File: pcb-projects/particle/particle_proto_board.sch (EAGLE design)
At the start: 38 parts, among them IC1 ATTINY20-MMH, IC2 DMC2400V, IC3 DMC2400V, J1 FTS-103-01-L-DV, SW1 T/S-PI SW, SW2 T/S-PI SW, SW3 T/S-PI SW

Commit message: closed #44, closed #43, closed #42
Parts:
- removed R11, R2: J5MM, jumper:J5MM
- removed R12: J15MM, jumper:J15MM
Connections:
- removed net N$17: IC3A.S, R11.1
- removed net N$2: R2.1, RXA.P
- net GND: now also IC3A.S; no longer R11.2
- net RX_A: now also RXA.P; no longer R2.2
- net VCC: no longer R12.1, R12.2
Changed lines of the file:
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@@
 <grid distance="0.1" unitdist="inch" unit="inch" style="lines" multiple="1" display="no" altdistance="0.01" altunitdist="inch" altunit="inch"/>
 <layers>
-<layer number="1" name="Top" color="4" fill="1" visible="yes" active="no"/>
-<layer number="16" name="Bottom" color="1" fill="1" visible="yes" active="no"/>
-<layer number="17" name="Pads" color="2" fill="1" visible="yes" active="no"/>
-<layer number="18" name="Vias" color="2" fill="1" visible="yes" active="no"/>
-<layer number="19" name="Unrouted" color="6" fill="1" visible="yes" active="no"/>
-<layer number="20" name="Dimension" color="15" fill="1" visible="yes" active="no"/>
-<layer number="21" name="tPlace" color="7" fill="1" visible="yes" active="no"/>
-<layer number="22" name="bPlace" color="7" fill="1" visible="yes" active="no"/>
-<layer number="23" name="tOrigins" color="15" fill="1" visible="yes" active="no"/>
-<layer number="24" name="bOrigins" color="15" fill="1" visible="yes" active="no"/>
-<layer number="25" name="tNames" color="7" fill="1" visible="yes" active="no"/>
-<layer number="26" name="bNames" color="7" fill="1" visible="yes" active="no"/>
-<layer number="27" name="tValues" color="7" fill="1" visible="yes" active="no"/>
-<layer number="28" name="bValues" color="7" fill="1" visible="yes" active="no"/>
+<layer number="1" name="Top" color="4" fill="1" visible="no" active="no"/>
+<layer number="16" name="Bottom" color="1" fill="1" visible="no" active="no"/>
+<layer number="17" name="Pads" color="2" fill="1" visible="no" active="no"/>
+<layer number="18" name="Vias" color="2" fill="1" visible="no" active="no"/>
+<layer number="19" name="Unrouted" color="6" fill="1" visible="no" active="no"/>
+<layer number="20" name="Dimension" color="15" fill="1" visible="no" active="no"/>
+<layer number="21" name="tPlace" color="7" fill="1" visible="no" active="no"/>
+<layer number="22" name="bPlace" color="7" fill="1" visible="no" active="no"/>
+<layer number="23" name="tOrigins" color="15" fill="1" visible="no" active="no"/>
+<layer number="24" name="bOrigins" color="15" fill="1" visible="no" active="no"/>
+<layer number="25" name="tNames" color="7" fill="1" visible="no" active="no"/>
+<layer number="26" name="bNames" color="7" fill="1" visible="no" active="no"/>
+<layer number="27" name="tValues" color="7" fill="1" visible="no" active="no"/>
+<layer number="28" name="bValues" color="7" fill="1" visible="no" active="no"/>
 <layer number="29" name="tStop" color="7" fill="3" visible="no" active="no"/>
 <layer number="30" name="bStop" color="7" fill="6" visible="no" active="no"/>
@@
 <layer number="35" name="tGlue" color="7" fill="4" visible="no" active="no"/>
 <layer number="36" name="bGlue" color="7" fill="5" visible="no" active="no"/>
-<layer number="37" name="tTest" color="7" fill="1" visible="yes" active="no"/>
-<layer number="38" name="bTest" color="7" fill="1" visible="yes" active="no"/>
+<layer number="37" name="tTest" color="7" fill="1" visible="no" active="no"/>
+<layer number="38" name="bTest" color="7" fill="1" visible="no" active="no"/>
 <layer number="39" name="tKeepout" color="4" fill="11" visible="no" active="no"/>
 <layer number="40" name="bKeepout" color="1" fill="11" visible="no" active="no"/>
@@
 <layer number="44" name="Drills" color="7" fill="1" visible="no" active="no"/>
 <layer number="45" name="Holes" color="7" fill="1" visible="no" active="no"/>
-<layer number="46" name="Milling" color="3" fill="1" visible="yes" active="no"/>
-<layer number="47" name="Measures" color="7" fill="1" visible="yes" active="no"/>
-<layer number="48" name="Document" color="7" fill="1" visible="yes" active="no"/>
-<layer number="49" name="Reference" color="7" fill="1" visible="yes" active="no"/>
-<layer number="50" name="dxf" color="7" fill="1" visible="yes" active="no"/>
-<layer number="51" name="tDocu" color="7" fill="1" visible="yes" active="no"/>
-<layer number="52" name="bDocu" color="7" fill="1" visible="yes" active="no"/>
-<layer number="53" name="tGND_GNDA" color="7" fill="9" visible="yes" active="no"/>
-<layer number="54" name="bGND_GNDA" color="1" fill="9" visible="yes" active="no"/>
-<layer number="56" name="wert" color="7" fill="1" visible="yes" active="no"/>
-<layer number="57" name="tCAD" color="7" fill="1" visible="yes" active="no"/>
+<layer number="46" name="Milling" color="3" fill="1" visible="no" active="no"/>
+<layer number="47" name="Measures" color="7" fill="1" visible="no" active="no"/>
+<layer number="48" name="Document" color="7" fill="1" visible="no" active="no"/>
+<layer number="49" name="Reference" color="7" fill="1" visible="no" active="no"/>
+<layer number="50" name="dxf" color="7" fill="1" visible="no" active="no"/>
+<layer number="51" name="tDocu" color="7" fill="1" visible="no" active="no"/>
+<layer number="52" name="bDocu" color="7" fill="1" visible="no" active="no"/>
+<layer number="53" name="tGND_GNDA" color="7" fill="9" visible="no" active="no"/>
+<layer number="54" name="bGND_GNDA" color="1" fill="9" visible="no" active="no"/>
+<layer number="56" name="wert" color="7" fill="1" visible="no" active="no"/>
+<layer number="57" name="tCAD" color="7" fill="1" visible="no" active="no"/>
 <layer number="90" name="Modules" color="5" fill="1" visible="yes" active="yes"/>
 <layer number="91" name="Nets" color="2" fill="1" visible="yes" active="yes"/>
@@
 <part name="PWR_LED" library="led" deviceset="LED" device="SML1206" value="RED"/>
 <part name="P+3" library="supply1" deviceset="VCC" device=""/>
-<part name="R11" library="jumper" deviceset="J" device="5MM" value=""/>
-<part name="P+5" library="supply1" deviceset="VCC" device=""/>
-<part name="P+7" library="supply1" deviceset="VCC" device=""/>
-<part name="R12" library="jumper" deviceset="J" device="15MM" value="J15MM"/>
 <part name="RESET" library="SparkFun-Electromechanical" deviceset="SWITCH-MOMENTARY-2" device="SMD"/>
 <part name="J1" library="samtec-FTS-103-01-L-DV" deviceset="FTS-103-01-L-DV" device=""/>
@@
 <part name="SW3" library="jumper-switches" deviceset="J2" device="X2MM" value="T/S-PI SW"/>
 <part name="SW2" library="jumper-switches" deviceset="J2" device="X2MM" value="T/S-PI SW"/>
-<part name="R2" library="jumper" deviceset="J" device="5MM" value="J5MM"/>
 </parts>
 <sheets>
@@
 <instance part="PWR_LED" gate="G$1" x="149.86" y="129.54"/>
 <instance part="P+3" gate="VCC" x="149.86" y="149.86"/>
-<instance part="R11" gate="1" x="297.18" y="86.36" rot="MR270"/>
-<instance part="P+5" gate="VCC" x="99.06" y="10.16" rot="R90"/>
-<instance part="P+7" gate="VCC" x="114.3" y="10.16" rot="R270"/>
-<instance part="R12" gate="1" x="106.68" y="10.16" rot="MR0"/>
 <instance part="RESET" gate="G$1" x="22.86" y="114.3" rot="R90"/>
 <instance part="J1" gate="A" x="124.46" y="48.26" rot="R180"/>
@@
 <instance part="SW3" gate="G$1" x="81.28" y="50.8" rot="R180"/>
 <instance part="SW2" gate="G$1" x="81.28" y="66.04" rot="R180"/>
-<instance part="R2" gate="1" x="241.3" y="147.32" rot="MR270"/>
 </instances>
 <busses>
@@
 </segment>
 <segment>
-<pinref part="R11" gate="1" pin="2"/>
 <pinref part="GND1" gate="1" pin="GND"/>
-<wire x1="297.18" y1="81.28" x2="297.18" y2="78.74" width="0.1524" layer="91"/>
+<pinref part="IC3" gate="A" pin="S"/>
+<wire x1="297.18" y1="93.98" x2="297.18" y2="78.74" width="0.1524" layer="91"/>
 </segment>
 <segment>
@@
 </segment>
 <segment>
-<pinref part="R12" gate="1" pin="1"/>
-<pinref part="P+7" gate="VCC" pin="VCC"/>
-</segment>
-<segment>
-<pinref part="R12" gate="1" pin="2"/>
-<pinref part="P+5" gate="VCC" pin="VCC"/>
-</segment>
-<segment>
 <pinref part="J1" gate="A" pin="2"/>
 <wire x1="106.68" y1="48.26" x2="104.14" y2="48.26" width="0.1524" layer="91"/>
@@
 <wire x1="210.82" y1="139.7" x2="210.82" y2="137.16" width="0.1524" layer="91"/>
 <junction x="210.82" y="137.16"/>
-<pinref part="R2" gate="1" pin="2"/>
-<wire x1="241.3" y1="137.16" x2="241.3" y2="142.24" width="0.1524" layer="91"/>
+<pinref part="RXA" gate="1" pin="P"/>
+<wire x1="241.3" y1="160.02" x2="241.3" y2="137.16" width="0.1524" layer="91"/>
 </segment>
 <segment>
@@
 </segment>
 </net>
-<net name="N$17" class="0">
-<segment>
-<pinref part="IC3" gate="A" pin="S"/>
-<pinref part="R11" gate="1" pin="1"/>
-<wire x1="297.18" y1="93.98" x2="297.18" y2="91.44" width="0.1524" layer="91"/>
-</segment>
-</net>
 <net name="N$23" class="0">
 <segment>
@@
 </segment>
 </net>
-<net name="N$2" class="0">
-<segment>
-<pinref part="RXA" gate="1" pin="P"/>
-<wire x1="241.3" y1="160.02" x2="241.3" y2="152.4" width="0.1524" layer="91"/>
-<pinref part="R2" gate="1" pin="1"/>
-</segment>
-</net>

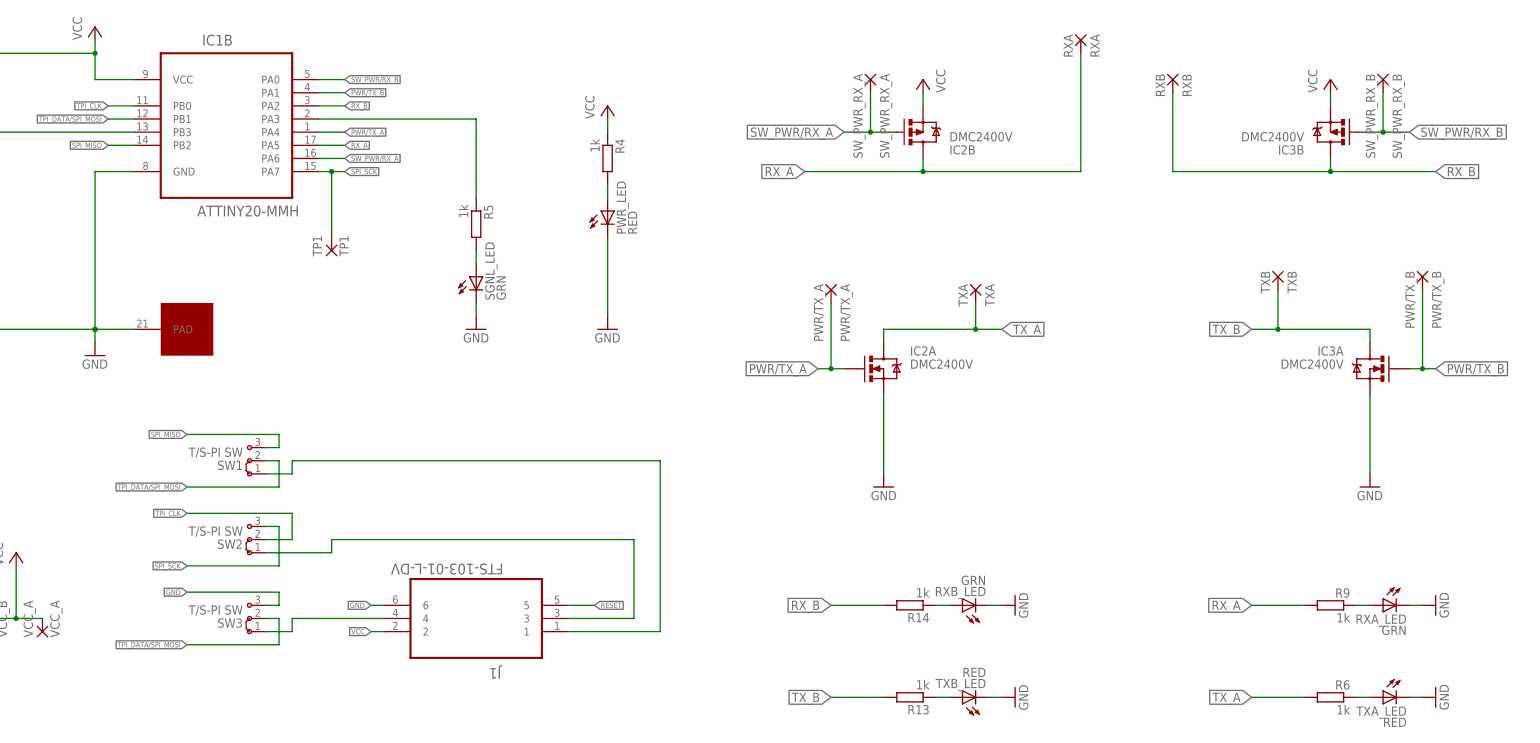
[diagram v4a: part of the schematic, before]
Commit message: renamed parts in schema
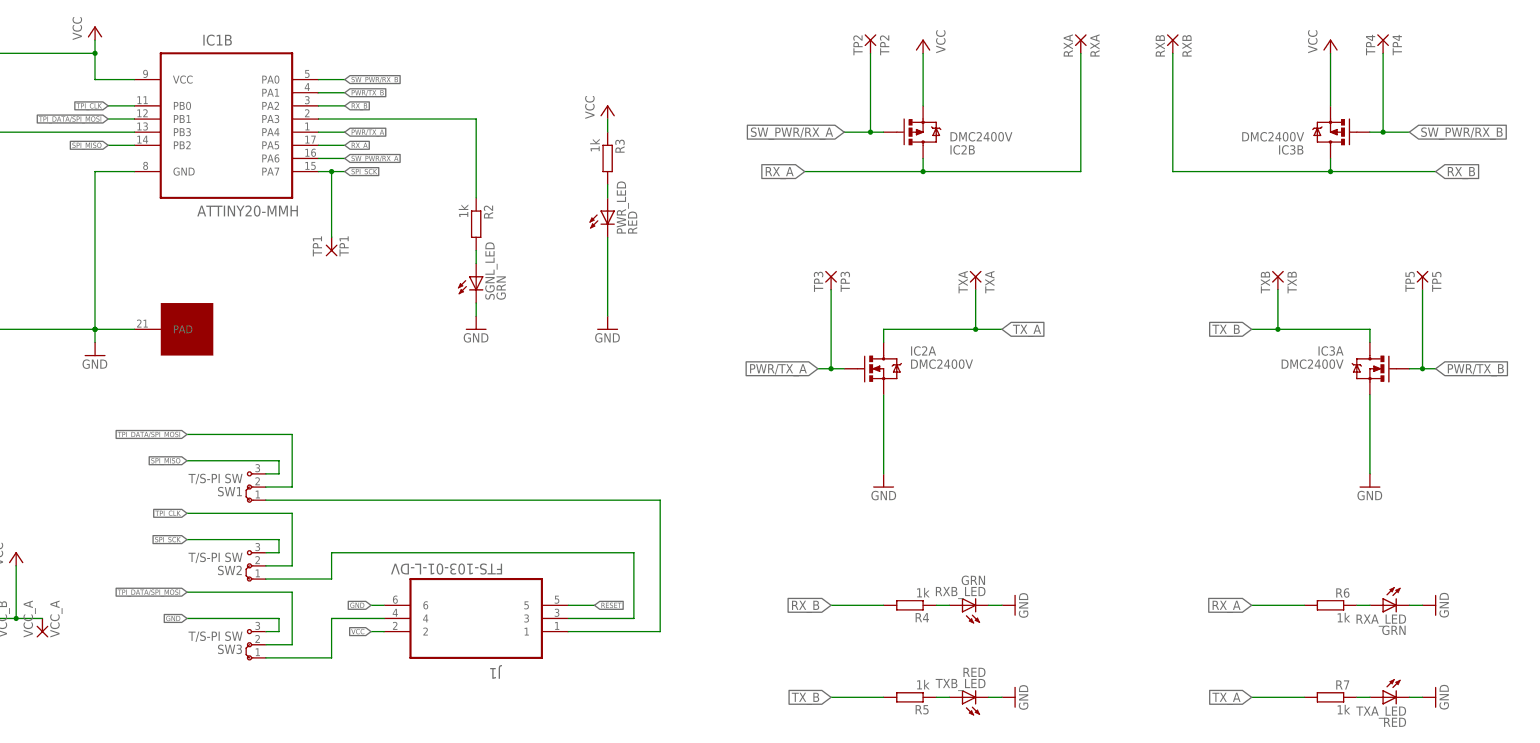
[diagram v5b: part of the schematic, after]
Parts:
- removed PWR/TX_A: PWR/TX_A, wirepad:1,6/0,9
- removed R13, R14, R9: 1k, rcl:R-EU_R1206
- removed SW_PWR_RX_A: SW_PWR_RX_A, wirepad:1,6/0,9
- removed SW_PWR_RX_B: SW_PWR_RX_B, wirepad:1,6/0,9
- added R2, R3, R7: 1k, rcl:R-EU_R1206
- added TP2: TP2, wirepad:1,6/0,9
- added TP3: TP3, wirepad:1,6/0,9
- added TP4: TP4, wirepad:1,6/0,9
- TP5: value PWR/TX_B -> TP5
- renumbered PWR/TX_B to TP5
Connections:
- net N$13: now also R5.1; no longer R13.1
- net N$18: now also R2.2; no longer R5.2
- net N$22: now also R3.2; no longer R4.2
- net N$23: now also R2.1; no longer R5.1
- net N$3: now also R7.1; no longer R6.1
- net N$4: now also R6.1; no longer R9.1
- net N$8: now also R4.1; no longer R14.1
- net PWR/TX_A: now also TP3.P; no longer PWR/TX_A.P
- net RX_A: now also R6.2; no longer R9.2
- net RX_B: now also R4.2; no longer R14.2
- net SW_PWR/RX_A: now also TP2.P; no longer SW_PWR_RX_A.P
- net SW_PWR/RX_B: now also TP4.P; no longer SW_PWR_RX_B.P
- net TX_A: now also R7.2; no longer R6.2
- net TX_B: now also R5.2; no longer R13.2
- net VCC: now also R3.1; no longer R4.1
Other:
- note added: "| TPI | SPI -------------- SW1 | 1-2 | 2-3 SW2 | 1-2 | 2-3 SW3 | 1-2 | 2-3"
- note removed: "SHUNTS"
- note removed: "| SPI | TPI -------------- SW1 | 2-3 | 1-2 SW2 | 2-3 | 1-2 SW3 | 2-3 | 1-2"
- moved on the sheet: R4, R5, R6, RXB, SW1, SW2, SW3, TXA

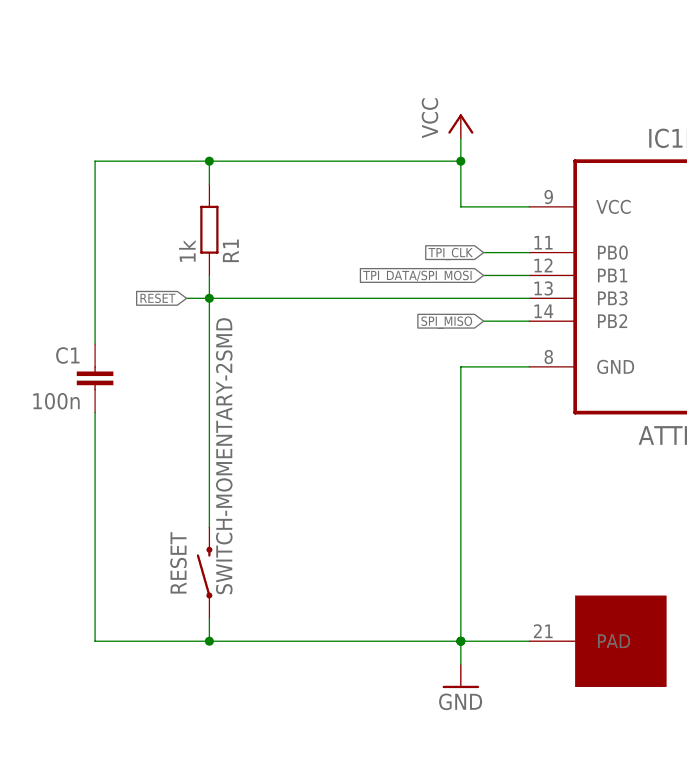
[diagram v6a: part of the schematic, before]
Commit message: created library for several smt switches (rs components)
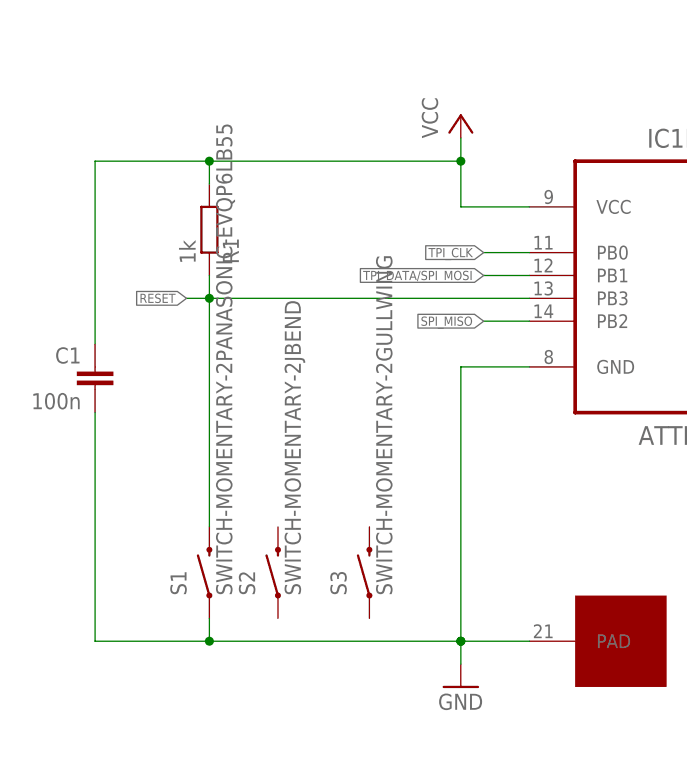
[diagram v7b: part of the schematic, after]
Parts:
- removed RESET: SWITCH-MOMENTARY-2SMD, SparkFun-Electromechanical:SWITCH-MOMENTARY-2SMD
- added S1: SWITCH-MOMENTARY-2PANASONIC-EVQP6LB55, ck-ksc-switches:SWITCH-MOMENTARY-2PANASONIC-EVQP6LB55
- added S2: SWITCH-MOMENTARY-2JBEND, rs-switches:SWITCH-MOMENTARY-2JBEND
- added S3: SWITCH-MOMENTARY-2GULLWING, rs-switches:SWITCH-MOMENTARY-2GULLWING
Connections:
- net GND: now also S1.1; no longer RESET.1
- net RESET: now also S1.2; no longer RESET.2
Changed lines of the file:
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@@
 <part name="PWR_LED" library="led" deviceset="LED" device="SML1206" value="RED"/>
 <part name="P+3" library="supply1" deviceset="VCC" device=""/>
-<part name="RESET" library="SparkFun-Electromechanical" deviceset="SWITCH-MOMENTARY-2" device="SMD"/>
 <part name="J1" library="samtec-FTS-103-01-L-DV" deviceset="FTS-103-01-L-DV" device=""/>
 <part name="SW1" library="jumper-switches" deviceset="J2" device="X2MM" value="T/S-PI SW"/>
 <part name="SW3" library="jumper-switches" deviceset="J2" device="X2MM" value="T/S-PI SW"/>
 <part name="SW2" library="jumper-switches" deviceset="J2" device="X2MM" value="T/S-PI SW"/>
+<part name="S1" library="ck-ksc-switches" deviceset="SWITCH-MOMENTARY-2" device="PANASONIC-EVQP6LB55"/>
+<part name="S2" library="rs-switches" deviceset="SWITCH-MOMENTARY-2" device="JBEND"/>
+<part name="S3" library="rs-switches" deviceset="SWITCH-MOMENTARY-2" device="" technology="GULLWING"/>
 </parts>
 <sheets>
@@
 <instance part="PWR_LED" gate="G$1" x="149.86" y="129.54"/>
 <instance part="P+3" gate="VCC" x="149.86" y="149.86"/>
-<instance part="RESET" gate="G$1" x="22.86" y="114.3" rot="R90"/>
 <instance part="J1" gate="A" x="124.46" y="48.26" rot="R180"/>
 <instance part="SW1" gate="G$1" x="81.28" y="76.2" rot="R180"/>
 <instance part="SW3" gate="G$1" x="81.28" y="45.72" rot="R180"/>
 <instance part="SW2" gate="G$1" x="81.28" y="60.96" rot="R180"/>
+<instance part="S1" gate="G$1" x="22.86" y="114.3" rot="R90"/>
+<instance part="S2" gate="G$1" x="30.48" y="114.3" rot="R90"/>
+<instance part="S3" gate="G$1" x="40.64" y="114.3" rot="R90"/>
 </instances>
 <busses>
@@
 <wire x1="50.8" y1="137.16" x2="58.42" y2="137.16" width="0.1524" layer="91"/>
 <wire x1="22.86" y1="109.22" x2="22.86" y2="106.68" width="0.1524" layer="91"/>
-<pinref part="RESET" gate="G$1" pin="1"/>
+<pinref part="S1" gate="G$1" pin="1"/>
 </segment>
 <segment>
@@
 <wire x1="22.86" y1="147.32" x2="22.86" y2="144.78" width="0.1524" layer="91"/>
 <junction x="22.86" y="144.78"/>
-<pinref part="RESET" gate="G$1" pin="2"/>
 <pinref part="IC1" gate="B" pin="PB3"/>
 <wire x1="22.86" y1="144.78" x2="58.42" y2="144.78" width="0.1524" layer="91"/>
-</segment>
-<segment>
+<pinref part="S1" gate="G$1" pin="2"/>
+</segment>
+<segment>
